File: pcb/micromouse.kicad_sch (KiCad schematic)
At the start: 43 parts, among them J10 B2B-PH-K-S, J11 B2B-PH-K-S, J13 B6B-ZR, J3 PINHD_1x4_Female, J6 PINHD_1x6_Female, J7 PINHD_1x8_Female, J8 PINHD_1x2_Female, J9 B6B-ZR, M1 Left, M2 Right, SW1 EG1218, SW3 Push_Button, U1 STM32F411RETx, U3 L293DD, U4 AZ1117-3.3, Y1 32.768 kHz 7 pF, Y2 25 MHz 10 pF

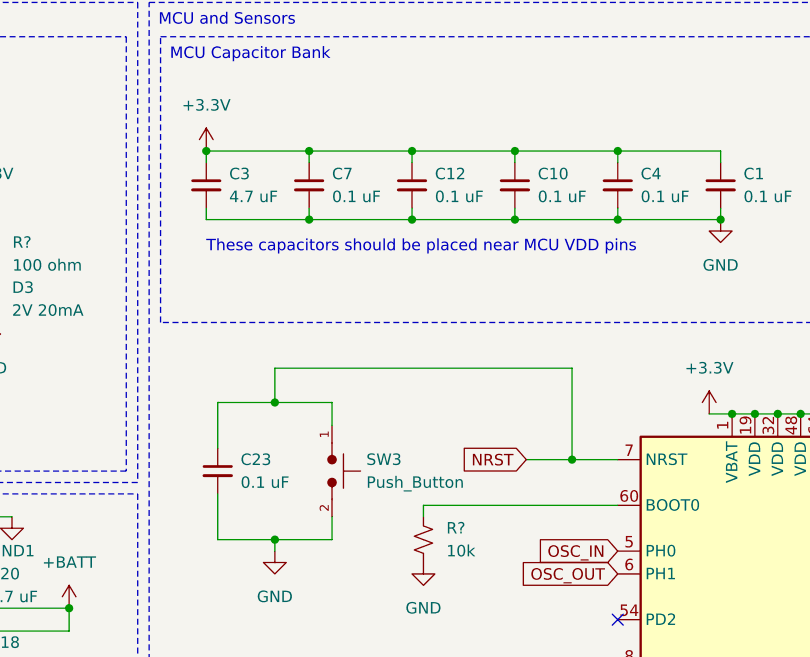
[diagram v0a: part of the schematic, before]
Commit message: Fixed PCB silkscreen, teardrops
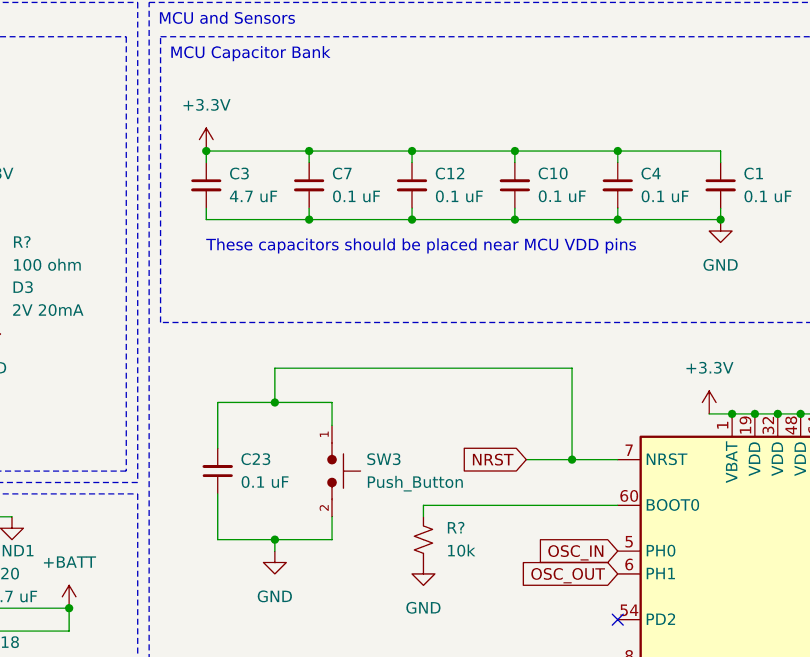
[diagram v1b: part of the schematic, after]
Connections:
- net +3.3V: now also C10.2; no longer C10.1
- net GND: now also C10.1, C23.1; no longer C10.2, C23.2
- net NRST: now also C23.2; no longer C23.1
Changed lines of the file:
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@@
+    )
+  )
+  (symbol (lib_id "Device:C_Small") (at 123.19 66.04 180) (unit 1)
+    (in_bom yes) (on_board yes) (dnp no) (fields_autoplaced)
+    (property "Reference" "C23" (at 125.73 64.7636 0)
+      (effects (font (size 1.27 1.27)) (justify right))
+    )
+    (property "Value" "0.1 uF" (at 125.73 67.3036 0)
+      (effects (font (size 1.27 1.27)) (justify right))
+    )
+    (property "Footprint" "Capacitor_SMD:C_0603_1608Metric" (at 123.19 66.04 0)
+      (effects (font (size 1.27 1.27)) hide)
+    )
+    (property "Datasheet" "~" (at 123.19 66.04 0)
+      (effects (font (size 1.27 1.27)) hide)
+    )
+    (pin "1")
+    (pin "2")
+    (instances
+      (project "micromouse"
+        (path "/77cbf270-6b61-4f1a-b1cd-1a823bc4a9d0"
+          (reference "C23") (unit 1)
+        )
+      )
+      (project "button"
+        (path "/91ddd5fd-ed4a-4a3f-ba4e-143f6c4541e0"
+          (reference "C15") (unit 1)
+        )
+      )
     )
   )
@@
         (path "/77cbf270-6b61-4f1a-b1cd-1a823bc4a9d0"
           (reference "#PWR04") (unit 1)
+        )
+      )
+    )
+  )
+  (symbol (lib_id "Device:C_Small") (at 156.21 34.29 180) (unit 1)
+    (in_bom yes) (on_board yes) (dnp no) (fields_autoplaced)
+    (property "Reference" "C10" (at 158.75 33.0136 0)
+      (effects (font (size 1.27 1.27)) (justify right))
+    )
+    (property "Value" "0.1 uF" (at 158.75 35.5536 0)
+      (effects (font (size 1.27 1.27)) (justify right))
+    )
+    (property "Footprint" "Capacitor_SMD:C_0603_1608Metric" (at 156.21 34.29 0)
+      (effects (font (size 1.27 1.27)) hide)
+    )
+    (property "Datasheet" "~" (at 156.21 34.29 0)
+      (effects (font (size 1.27 1.27)) hide)
+    )
+    (pin "1")
+    (pin "2")
+    (instances
+      (project "micromouse"
+        (path "/77cbf270-6b61-4f1a-b1cd-1a823bc4a9d0"
+          (reference "C10") (unit 1)
         )
       )
@@
     )
   )
-  (symbol (lib_id "Device:C_Small") (at 123.19 66.04 0) (unit 1)
-    (in_bom yes) (on_board yes) (dnp no) (fields_autoplaced)
-    (property "Reference" "C23" (at 125.73 64.7763 0)
-      (effects (font (size 1.27 1.27)) (justify left))
-    )
-    (property "Value" "0.1 uF" (at 125.73 67.3163 0)
-      (effects (font (size 1.27 1.27)) (justify left))
-    )
-    (property "Footprint" "Capacitor_SMD:C_0603_1608Metric" (at 123.19 66.04 0)
-      (effects (font (size 1.27 1.27)) hide)
-    )
-    (property "Datasheet" "~" (at 123.19 66.04 0)
-      (effects (font (size 1.27 1.27)) hide)
-    )
-    (pin "1")
-    (pin "2")
-    (instances
-      (project "micromouse"
-        (path "/77cbf270-6b61-4f1a-b1cd-1a823bc4a9d0"
-          (reference "C23") (unit 1)
-        )
-      )
-      (project "button"
-        (path "/91ddd5fd-ed4a-4a3f-ba4e-143f6c4541e0"
-          (reference "C15") (unit 1)
-        )
-      )
-    )
-  )
   (symbol (lib_id "power:+3.3V") (at 177.8 59.69 0) (unit 1)
     (in_bom yes) (on_board yes) (dnp no)
@@
         )
       )
-    )
-  )
-  (symbol (lib_id "Device:C_Small") (at 156.21 34.29 0) (unit 1)
-    (in_bom yes) (on_board yes) (dnp no) (fields_autoplaced)
-    (property "Reference" "C10" (at 158.75 33.0263 0)
-      (effects (font (size 1.27 1.27)) (justify left))
-    )
-    (property "Value" "0.1 uF" (at 158.75 35.5663 0)
-      (effects (font (size 1.27 1.27)) (justify left))
-    )
-    (property "Footprint" "Capacitor_SMD:C_0603_1608Metric" (at 156.21 34.29 0)
-      (effects (font (size 1.27 1.27)) hide)
-    )
-    (property "Datasheet" "~" (at 156.21 34.29 0)
-      (effects (font (size 1.27 1.27)) hide)
-    )
-    (pin "1")
-    (pin "2")
-    (instances
-      (project "micromouse"
-        (path "/77cbf270-6b61-4f1a-b1cd-1a823bc4a9d0"
-          (reference "C10") (unit 1)
-        )
-      )
